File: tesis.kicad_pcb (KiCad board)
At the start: 2 copper layers, 12 parts, among them J1 Connector_RJ10, J2 Connector_RJ10, J3 Connector_RJ10, J4 Connector_RJ10, J5 Connector_RJ10, J6 Connector_RJ10, J7 Connector_RJ10, J8 Connector_RJ10, U1 ESP32-WROOM, U2 Interface_Expansion_PCF8574, U3 Interface_Expansion_TCA9548AP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

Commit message: Agrego v1.0 de SmartSaffron
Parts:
- removed J2, J3, J4, J5, J6, J7, J8: Connector_RJ10, 00_lib_fp:4P4C_narrow
- removed MOD1: RPi_GPIO, 00_lib_fp:RPi_fp
- removed U3: Interface_Expansion_TCA9548APWR, Package_SO:TSSOP-24_4.4x7.8mm_P0.65mm
- added AE501: Antenna_Shield, 00_lib_fp:U.FL_Molex_MCRF_73412-0110_Vertical, B.Cu at (62.4, 58.0)
- added BT501: CR2032, 00_lib_fp:BatteryHolder_ComfortableElectronic_CH273-2450_1x2450, F.Cu at (153.5, 80.8)
- added BT502: Battery_Cell, 00_lib_fp:BatteryHolder_Seiko_MS621F, B.Cu at (96.2, 66.2)
- added BZ601: Buzzer, 00_lib_fp:Buzzer_23x10, F.Cu at (167.1, 56.1)
- added C1: 10u, 00_lib_fp:C_0805_2012Metric_Pad1.18x1.45mm_HandSolder, B.Cu at (95.2, 127.3)
- added C101: 470uF/50V, 00_lib_fp:CP_Elec_10x10, F.Cu at (80.0, 126.7)
- added C102: 33u, 00_lib_fp:C_0805_2012Metric_Pad1.18x1.45mm_HandSolder, B.Cu at (97.6, 99.5)
- added C103: 470uF/50V, 00_lib_fp:CP_Elec_8x10.5, F.Cu at (87.9, 75.4)
- added C104: 470u/50V, 00_lib_fp:CP_Elec_8x10.5, F.Cu at (85.4, 115.9)
- added C105: 1u, 00_lib_fp:C_0805_2012Metric_Pad1.18x1.45mm_HandSolder, F.Cu at (85.4, 110.2)
- added C106: 33u, 00_lib_fp:C_0805_2012Metric_Pad1.18x1.45mm_HandSolder, B.Cu at (78.6, 99.4)
- added C107: 470uF/50V, 00_lib_fp:CP_Elec_8x10.5, F.Cu at (67.6, 75.4)
- added C108: 470uF/50V, 00_lib_fp:CP_Elec_8x10.5, F.Cu at (70.9, 115.9)
- added C109: 1u, 00_lib_fp:C_0805_2012Metric_Pad1.18x1.45mm_HandSolder, F.Cu at (69.9, 110.2)
- added C2: 100n, 00_lib_fp:C_0805_2012Metric_Pad1.18x1.45mm_HandSolder, B.Cu at (97.3, 127.3)
- added C201: 10u, 00_lib_fp:C_0805_2012Metric_Pad1.18x1.45mm_HandSolder, B.Cu at (170.9, 93.4)
- added C202: 100n, 00_lib_fp:C_0805_2012Metric_Pad1.18x1.45mm_HandSolder, B.Cu at (170.9, 91.0)
- added C3: 100n, 00_lib_fp:C_0805_2012Metric_Pad1.18x1.45mm_HandSolder, B.Cu at (92.1, 124.5)
- added C301: 100n, 00_lib_fp:C_0805_2012Metric_Pad1.18x1.45mm_HandSolder, F.Cu at (120.1, 50.1)
- added C302: 100n, 00_lib_fp:C_0805_2012Metric_Pad1.18x1.45mm_HandSolder, B.Cu at (144.5, 83.2)
- added C303: 100n, 00_lib_fp:C_0805_2012Metric_Pad1.18x1.45mm_HandSolder, B.Cu at (141.1, 92.4)
- added C304: 10u, 00_lib_fp:C_0805_2012Metric_Pad1.18x1.45mm_HandSolder, F.Cu at (118.6, 44.8)
- added C305: 100n, 00_lib_fp:C_0805_2012Metric_Pad1.18x1.45mm_HandSolder, F.Cu at (121.6, 44.8)
- added C401: 100n, 00_lib_fp:C_0805_2012Metric_Pad1.18x1.45mm_HandSolder, B.Cu at (116.7, 139.7)
- added C402: 100n, 00_lib_fp:C_0805_2012Metric_Pad1.18x1.45mm_HandSolder, B.Cu at (121.8, 139.7)
- added C403: 100n, 00_lib_fp:C_0805_2012Metric_Pad1.18x1.45mm_HandSolder, B.Cu at (126.3, 139.7)
- added C404: 100n, 00_lib_fp:C_0805_2012Metric_Pad1.18x1.45mm_HandSolder, B.Cu at (131.4, 139.7)
- added C405: 10u, 00_lib_fp:C_0805_2012Metric_Pad1.18x1.45mm_HandSolder, F.Cu at (108.6, 95.3)
- added C406: 100n, 00_lib_fp:C_0805_2012Metric_Pad1.18x1.45mm_HandSolder, F.Cu at (105.6, 95.3)
- added C407: 100n, 00_lib_fp:C_0805_2012Metric_Pad1.18x1.45mm_HandSolder, B.Cu at (136.9, 139.7)
- added C408: 100n, 00_lib_fp:C_0805_2012Metric_Pad1.18x1.45mm_HandSolder, B.Cu at (142.1, 139.7)
- added C409: 100n, 00_lib_fp:C_0805_2012Metric_Pad1.18x1.45mm_HandSolder, B.Cu at (147.2, 139.7)
- added C410: 100n, 00_lib_fp:C_0805_2012Metric_Pad1.18x1.45mm_HandSolder, B.Cu at (152.1, 139.7)
- added C501: 10u, 00_lib_fp:C_0805_2012Metric_Pad1.18x1.45mm_HandSolder, B.Cu at (179.0, 67.2)
- added C502: 100n, 00_lib_fp:C_0805_2012Metric_Pad1.18x1.45mm_HandSolder, B.Cu at (176.9, 67.2)
- added C503: 10u, 00_lib_fp:C_0805_2012Metric_Pad1.18x1.45mm_HandSolder, B.Cu at (175.2, 71.6)
- added C504: 100n, 00_lib_fp:C_0805_2012Metric_Pad1.18x1.45mm_HandSolder, B.Cu at (175.2, 73.8)
- added C505: 10u, 00_lib_fp:C_0805_2012Metric_Pad1.18x1.45mm_HandSolder, B.Cu at (77.9, 75.7)
- added C506: 100n, 00_lib_fp:C_0805_2012Metric_Pad1.18x1.45mm_HandSolder, B.Cu at (77.9, 73.4)
- added D101: DF06S, 00_lib_fp:Diode_Bridge_Vishay_DFSFlat, B.Cu at (79.3, 134.6)
- added D102: 1N5824, 00_lib_fp:D_SMB_Handsoldering, F.Cu at (95.1, 115.7)
- added D103: green, 00_lib_fp:LED_0805_2012Metric_Castellated, F.Cu at (87.4, 69.0)
- added D104: 1N5824, 00_lib_fp:D_SMB_Handsoldering, F.Cu at (61.9, 115.5)
- added D105: green, 00_lib_fp:LED_0805_2012Metric_Castellated, F.Cu at (75.9, 69.0)
- added D301: WS2812, 00_lib_fp:LED_WS2812_PLCC6_5.0x5.0mm_P1.6mm, B.Cu at (134.4, 83.9)
- added D302: WS2812, 00_lib_fp:LED_WS2812_PLCC6_5.0x5.0mm_P1.6mm, B.Cu at (134.4, 92.9)
- added D501: 1N5817, 00_lib_fp:D_MiniMELF_Handsoldering, B.Cu at (94.3, 71.5)
- added D502: LED, 00_lib_fp:LED_0805_2012Metric_Castellated, B.Cu at (70.5, 69.8)
- added G1: LOGO_SSaffron, 00_lib_fp:smart_saffron, F.Cu at (85.3, 53.2)
- added G2: LOGO_utn, 00_lib_fp:logo_utn, F.Cu at (117.2, 70.5)
- added G3: LOGO_azafran, 00_lib_fp:azafran, F.Cu at (134.1, 86.6)
- added G4: LOGO_arg, 00_lib_fp:argentina, F.Cu at (92.1, 134.2)
- added J201: RJ10, 00_lib_fp:4P4C_narrow, F.Cu at (197.1, 100.6)
- added J202: RJ10, 00_lib_fp:4P4C_narrow, F.Cu at (197.1, 87.9)
- added J203: RJ10, 00_lib_fp:4P4C_narrow, F.Cu at (197.1, 75.7)
- added J204: RJ10, 00_lib_fp:4P4C_narrow, F.Cu at (197.1, 63.5)
- added J205: RJ10, 00_lib_fp:4P4C_narrow, F.Cu at (197.1, 51.2)
- added J206: RJ10, 00_lib_fp:4P4C_narrow, F.Cu at (197.1, 113.0)
- added J207: RJ10, 00_lib_fp:4P4C_narrow, F.Cu at (197.1, 125.5)
- added J208: RJ10, 00_lib_fp:4P4C_narrow, F.Cu at (197.1, 137.7)
- added J301: BOOT_Mode, 00_lib_fp:PinHeader_1x02_P2.54mm_Vertical, F.Cu at (151.4, 63.5)
- added J302: Debug_PROG, 00_lib_fp:PinHeader_1x03_P2.54mm_Vertical, F.Cu at (150.9, 48.3)
- added J401: OUTPUT_SW, 00_lib_fp:TerminalBlock_Phoenix_MKDS-1,5-8-5.08_1x08_P5.08mm_Horizontal, F.Cu at (116.9, 133.7)
- added J402: COMMON, 00_lib_fp:TerminalBlock_Phoenix_MKDS-1,5-2-5.08_1x02_P5.08mm_Horizontal, F.Cu at (101.8, 133.7)
- added J602: Lights, 00_lib_fp:TerminalBlock_Phoenix_MKDS-1,5-4-5.08_1x04_P5.08mm_Horizontal, F.Cu at (162.9, 133.7)
- added JP1: jumper, 00_lib_fp:SolderJumper-2_P1.3mm_Open_RoundedPad1.0x1.5mm, B.Cu at (91.7, 137.0)
- added JP101: jumper, 00_lib_fp:SolderJumper-2_P1.3mm_Open_RoundedPad1.0x1.5mm, B.Cu at (99.2, 83.7)
- added JP102: jumper, 00_lib_fp:SolderJumper-2_P1.3mm_Open_RoundedPad1.0x1.5mm, B.Cu at (99.2, 77.9)
- added JP103: jumper, 00_lib_fp:SolderJumper-2_P1.3mm_Open_RoundedPad1.0x1.5mm, B.Cu at (99.2, 86.4)
- added JP104: jumper, 00_lib_fp:SolderJumper-2_P1.3mm_Open_RoundedPad1.0x1.5mm, B.Cu at (99.2, 92.0)
- added JP2: jumper, 00_lib_fp:SolderJumper-2_P1.3mm_Open_RoundedPad1.0x1.5mm, B.Cu at (91.8, 140.3)
- added L101: 33uH/5A, 00_lib_fp:Coil_ferrite, F.Cu at (86.9, 87.9)
- added L102: 33uH/5A, 00_lib_fp:Coil_ferrite, F.Cu at (67.1, 87.9)
- added L501: 27u, 00_lib_fp:L_0805_2012Metric_Pad1.15x1.40mm_HandSolder, B.Cu at (68.8, 59.1)
- added MH1: MountingHole, 00_lib_fp:MountingHole_3.2mm_M3_Pad_Via, F.Cu at (63.6, 138.7)
- added MH2: MountingHole, 00_lib_fp:MountingHole_3.2mm_M3_Pad_Via, F.Cu at (190.6, 138.7)
- added MH3: MountingHole, 00_lib_fp:MountingHole_3.2mm_M3_Pad_Via, F.Cu at (64.1, 65.7)
- added MH4: MountingHole, 00_lib_fp:MountingHole_3.2mm_M3_Pad_Via, F.Cu at (190.6, 46.7)
- added MOD301: RPi_GPIO, 00_lib_fp:PinSocket_2x20_P2.54mm_Vertical_SMD, B.Cu at (86.9, 48.8)
- added Q401: bss138, 00_lib_fp:SOT-23, B.Cu at (102.9, 116.9)
- added Q402: bss138, 00_lib_fp:SOT-23, B.Cu at (111.5, 116.9)
- added Q403: mac97a8, 00_lib_fp:TO-92_Inline, F.Cu at (101.6, 127.7)
- added Q404: mac97a8, 00_lib_fp:TO-92_Inline, F.Cu at (110.4, 127.7)
- added Q405: bss138, 00_lib_fp:SOT-23, B.Cu at (120.3, 116.9)
- added Q406: bss138, 00_lib_fp:SOT-23, B.Cu at (128.7, 116.9)
- added Q407: mac97a8, 00_lib_fp:TO-92_Inline, F.Cu at (119.0, 127.7)
- added Q408: mac97a8, 00_lib_fp:TO-92_Inline, F.Cu at (127.4, 127.7)
- added Q409: bss138, 00_lib_fp:SOT-23, B.Cu at (137.2, 116.9)
- added Q410: bss138, 00_lib_fp:SOT-23, B.Cu at (145.8, 116.9)
- added Q411: mac97a8, 00_lib_fp:TO-92_Inline, F.Cu at (135.9, 127.7)
- added Q412: mac97a8, 00_lib_fp:TO-92_Inline, F.Cu at (144.5, 127.7)
- added Q413: bss138, 00_lib_fp:SOT-23, B.Cu at (154.4, 116.9)
- added Q414: bss138, 00_lib_fp:SOT-23, B.Cu at (162.8, 116.9)
- added Q415: mac97a8, 00_lib_fp:TO-92_Inline, F.Cu at (153.1, 127.7)
- added Q416: mac97a8, 00_lib_fp:TO-92_Inline, F.Cu at (161.7, 127.7)
- added Q601: bss138, 00_lib_fp:SOT-23, F.Cu at (161.2, 94.5)
- added Q602: mac97a8, 00_lib_fp:TO-92_Inline, F.Cu at (174.5, 127.7)
- added Q603: bss138, 00_lib_fp:SOT-23, F.Cu at (166.2, 94.5)
- added Q604: bss138, 00_lib_fp:SOT-23, B.Cu at (168.7, 55.7)
- added Q605: mac97a8, 00_lib_fp:TO-92_Inline, F.Cu at (168.4, 127.7)
- added Q606: bss138, 00_lib_fp:SOT-23, F.Cu at (171.2, 94.5)
- added Q607: mac97a8, 00_lib_fp:TO-92_Inline, F.Cu at (180.6, 127.7)
- added R1: R, 00_lib_fp:R_0805_2012Metric_Pad1.20x1.40mm_HandSolder, B.Cu at (94.0, 122.4)
- added R101: 1k5, 00_lib_fp:R_0805_2012Metric_Pad1.20x1.40mm_HandSolder, B.Cu at (81.6, 93.7)
- added R102: 0, 00_lib_fp:R_0805_2012Metric_Pad1.20x1.40mm_HandSolder, B.Cu at (85.7, 93.7)
- added R103: 0, 00_lib_fp:R_0805_2012Metric_Pad1.20x1.40mm_HandSolder, B.Cu at (81.6, 91.5)
- added R104: 8k2, 00_lib_fp:R_0805_2012Metric_Pad1.20x1.40mm_HandSolder, B.Cu at (89.7, 93.7)
- added R105: 2k2, 00_lib_fp:R_0805_2012Metric_Pad1.20x1.40mm_HandSolder, F.Cu at (83.6, 68.9)
- added R106: 4k7, 00_lib_fp:R_0805_2012Metric_Pad1.20x1.40mm_HandSolder, B.Cu at (62.1, 93.7)
- added R107: 0, 00_lib_fp:R_0805_2012Metric_Pad1.20x1.40mm_HandSolder, B.Cu at (66.1, 93.7)
- added R108: 0, 00_lib_fp:R_0805_2012Metric_Pad1.20x1.40mm_HandSolder, B.Cu at (62.1, 91.5)
- added R109: 15k, 00_lib_fp:R_0805_2012Metric_Pad1.20x1.40mm_HandSolder, B.Cu at (70.1, 93.7)
- added R110: 2k2, 00_lib_fp:R_0805_2012Metric_Pad1.20x1.40mm_HandSolder, F.Cu at (72.4, 68.9)
- added R2: R, 00_lib_fp:R_0805_2012Metric_Pad1.20x1.40mm_HandSolder, B.Cu at (94.0, 120.4)
- added R201: 10k, 00_lib_fp:R_0805_2012Metric_Pad1.20x1.40mm_HandSolder, B.Cu at (190.5, 100.1)
- added R202: 10k, 00_lib_fp:R_0805_2012Metric_Pad1.20x1.40mm_HandSolder, B.Cu at (190.5, 98.0)
- added R203: 10k, 00_lib_fp:R_0805_2012Metric_Pad1.20x1.40mm_HandSolder, B.Cu at (190.6, 87.6)
- added R204: 10k, 00_lib_fp:R_0805_2012Metric_Pad1.20x1.40mm_HandSolder, B.Cu at (190.6, 85.6)
- added R205: 10k, 00_lib_fp:R_0805_2012Metric_Pad1.20x1.40mm_HandSolder, B.Cu at (190.6, 75.2)
- added R206: 10k, 00_lib_fp:R_0805_2012Metric_Pad1.20x1.40mm_HandSolder, B.Cu at (190.6, 73.2)
- added R207: 4k7, 00_lib_fp:R_0805_2012Metric_Pad1.20x1.40mm_HandSolder, B.Cu at (186.0, 90.5)
- added R208: 4k7, 00_lib_fp:R_0805_2012Metric_Pad1.20x1.40mm_HandSolder, B.Cu at (183.9, 90.5)
- added R209: 10k, 00_lib_fp:R_0805_2012Metric_Pad1.20x1.40mm_HandSolder, B.Cu at (190.6, 63.0)
- added R210: 10k, 00_lib_fp:R_0805_2012Metric_Pad1.20x1.40mm_HandSolder, B.Cu at (190.6, 60.9)
- added R211: 10k, 00_lib_fp:R_0805_2012Metric_Pad1.20x1.40mm_HandSolder, F.Cu at (175.3, 97.4)
- added R212: 10k, 00_lib_fp:R_0805_2012Metric_Pad1.20x1.40mm_HandSolder, F.Cu at (177.2, 92.2)
- added R213: 10k, 00_lib_fp:R_0805_2012Metric_Pad1.20x1.40mm_HandSolder, F.Cu at (177.2, 95.1)
- added R214: 10k, 00_lib_fp:R_0805_2012Metric_Pad1.20x1.40mm_HandSolder, F.Cu at (177.2, 89.1)
- added R215: 10k, 00_lib_fp:R_0805_2012Metric_Pad1.20x1.40mm_HandSolder, B.Cu at (190.6, 54.2)
- added R216: 10k, 00_lib_fp:R_0805_2012Metric_Pad1.20x1.40mm_HandSolder, B.Cu at (190.6, 52.2)
- added R217: 10k, 00_lib_fp:R_0805_2012Metric_Pad1.20x1.40mm_HandSolder, F.Cu at (179.2, 92.2)
- added R218: 10k, 00_lib_fp:R_0805_2012Metric_Pad1.20x1.40mm_HandSolder, F.Cu at (179.2, 95.1)
- added R219: 10k, 00_lib_fp:R_0805_2012Metric_Pad1.20x1.40mm_HandSolder, F.Cu at (179.2, 89.1)
- added R220: 10k, 00_lib_fp:R_0805_2012Metric_Pad1.20x1.40mm_HandSolder, B.Cu at (190.5, 112.4)
- added R221: 10k, 00_lib_fp:R_0805_2012Metric_Pad1.20x1.40mm_HandSolder, B.Cu at (190.5, 110.4)
- added R222: 10k, 00_lib_fp:R_0805_2012Metric_Pad1.20x1.40mm_HandSolder, B.Cu at (190.6, 125.0)
- added R223: 10k, 00_lib_fp:R_0805_2012Metric_Pad1.20x1.40mm_HandSolder, B.Cu at (190.6, 123.0)
- added R224: 10k, 00_lib_fp:R_0805_2012Metric_Pad1.20x1.40mm_HandSolder, B.Cu at (190.6, 133.2)
- added R225: 10k, 00_lib_fp:R_0805_2012Metric_Pad1.20x1.40mm_HandSolder, B.Cu at (190.6, 131.2)
- added R301: 10k, 00_lib_fp:R_0805_2012Metric_Pad1.20x1.40mm_HandSolder, F.Cu at (120.2, 47.9)
- added R401: 1k, 00_lib_fp:R_0805_2012Metric_Pad1.20x1.40mm_HandSolder, B.Cu at (100.0, 123.9)
- added R402: 1k, 00_lib_fp:R_0805_2012Metric_Pad1.20x1.40mm_HandSolder, B.Cu at (108.8, 123.9)
- added R403: 470, 00_lib_fp:R_0805_2012Metric_Pad1.20x1.40mm_HandSolder, B.Cu at (116.6, 137.5)
- added R404: 470, 00_lib_fp:R_0805_2012Metric_Pad1.20x1.40mm_HandSolder, B.Cu at (121.8, 137.5)
- added R405: 1k, 00_lib_fp:R_0805_2012Metric_Pad1.20x1.40mm_HandSolder, B.Cu at (105.0, 110.1)
- added R406: 470, 00_lib_fp:R_0805_2012Metric_Pad1.20x1.40mm_HandSolder, B.Cu at (100.7, 110.1)
- added R407: 1k, 00_lib_fp:R_0805_2012Metric_Pad1.20x1.40mm_HandSolder, B.Cu at (113.8, 110.1)
- added R408: 470, 00_lib_fp:R_0805_2012Metric_Pad1.20x1.40mm_HandSolder, B.Cu at (109.4, 110.1)
- added R409: 4k7, 00_lib_fp:R_0805_2012Metric_Pad1.20x1.40mm_HandSolder, F.Cu at (112.9, 85.6)
- added R410: 4k7, 00_lib_fp:R_0805_2012Metric_Pad1.20x1.40mm_HandSolder, F.Cu at (115.0, 85.6)
- added R411: 10k, 00_lib_fp:R_0805_2012Metric_Pad1.20x1.40mm_HandSolder, F.Cu at (108.4, 103.4)
- added R412: 10k, 00_lib_fp:R_0805_2012Metric_Pad1.20x1.40mm_HandSolder, F.Cu at (105.6, 103.4)
- added R413: 10k, 00_lib_fp:R_0805_2012Metric_Pad1.20x1.40mm_HandSolder, F.Cu at (102.8, 103.4)
- added R414: 10k, 00_lib_fp:R_0805_2012Metric_Pad1.20x1.40mm_HandSolder, F.Cu at (108.4, 105.4)
- added R415: 10k, 00_lib_fp:R_0805_2012Metric_Pad1.20x1.40mm_HandSolder, F.Cu at (105.6, 105.4)
- added R416: 10k, 00_lib_fp:R_0805_2012Metric_Pad1.20x1.40mm_HandSolder, F.Cu at (102.8, 105.4)
- added R417: 1k, 00_lib_fp:R_0805_2012Metric_Pad1.20x1.40mm_HandSolder, B.Cu at (117.4, 123.9)
- added R418: 1k, 00_lib_fp:R_0805_2012Metric_Pad1.20x1.40mm_HandSolder, B.Cu at (125.8, 123.9)
- added R419: 470, 00_lib_fp:R_0805_2012Metric_Pad1.20x1.40mm_HandSolder, B.Cu at (126.2, 137.5)
- added R420: 470, 00_lib_fp:R_0805_2012Metric_Pad1.20x1.40mm_HandSolder, B.Cu at (131.4, 137.6)
- added R421: 1k, 00_lib_fp:R_0805_2012Metric_Pad1.20x1.40mm_HandSolder, B.Cu at (122.4, 110.1)
- added R422: 470, 00_lib_fp:R_0805_2012Metric_Pad1.20x1.40mm_HandSolder, B.Cu at (118.2, 110.1)
- added R423: 1k, 00_lib_fp:R_0805_2012Metric_Pad1.20x1.40mm_HandSolder, B.Cu at (130.8, 110.1)
- added R424: 470, 00_lib_fp:R_0805_2012Metric_Pad1.20x1.40mm_HandSolder, B.Cu at (126.6, 110.1)
- added R425: 1k, 00_lib_fp:R_0805_2012Metric_Pad1.20x1.40mm_HandSolder, B.Cu at (134.3, 123.9)
- added R426: 1k, 00_lib_fp:R_0805_2012Metric_Pad1.20x1.40mm_HandSolder, B.Cu at (142.9, 123.9)
- added R427: 470, 00_lib_fp:R_0805_2012Metric_Pad1.20x1.40mm_HandSolder, B.Cu at (136.9, 137.6)
- added R428: 470, 00_lib_fp:R_0805_2012Metric_Pad1.20x1.40mm_HandSolder, B.Cu at (142.1, 137.5)
- added R429: 1k, 00_lib_fp:R_0805_2012Metric_Pad1.20x1.40mm_HandSolder, B.Cu at (139.4, 110.1)
- added R430: 470, 00_lib_fp:R_0805_2012Metric_Pad1.20x1.40mm_HandSolder, B.Cu at (135.0, 110.1)
- added R431: 1k, 00_lib_fp:R_0805_2012Metric_Pad1.20x1.40mm_HandSolder, B.Cu at (147.9, 110.1)
- added R432: 470, 00_lib_fp:R_0805_2012Metric_Pad1.20x1.40mm_HandSolder, B.Cu at (143.6, 110.1)
- added R433: 1k, 00_lib_fp:R_0805_2012Metric_Pad1.20x1.40mm_HandSolder, B.Cu at (151.6, 123.9)
- added R434: 1k, 00_lib_fp:R_0805_2012Metric_Pad1.20x1.40mm_HandSolder, B.Cu at (160.1, 123.9)
- added R435: 470, 00_lib_fp:R_0805_2012Metric_Pad1.20x1.40mm_HandSolder, B.Cu at (147.2, 137.6)
- added R436: 470, 00_lib_fp:R_0805_2012Metric_Pad1.20x1.40mm_HandSolder, B.Cu at (152.1, 137.6)
- added R437: 1k, 00_lib_fp:R_0805_2012Metric_Pad1.20x1.40mm_HandSolder, B.Cu at (156.3, 110.1)
- added R438: 470, 00_lib_fp:R_0805_2012Metric_Pad1.20x1.40mm_HandSolder, B.Cu at (152.2, 110.1)
- added R439: 1k, 00_lib_fp:R_0805_2012Metric_Pad1.20x1.40mm_HandSolder, B.Cu at (165.1, 110.1)
- added R440: 470, 00_lib_fp:R_0805_2012Metric_Pad1.20x1.40mm_HandSolder, B.Cu at (160.8, 110.1)
- added R501: 1k, 00_lib_fp:R_0805_2012Metric_Pad1.20x1.40mm_HandSolder, B.Cu at (156.3, 61.4)
- added R502: 1k, 00_lib_fp:R_0805_2012Metric_Pad1.20x1.40mm_HandSolder, B.Cu at (158.9, 61.4)
- added R503: 10.5, 00_lib_fp:R_0805_2012Metric_Pad1.20x1.40mm_HandSolder, B.Cu at (72.0, 60.3)
- added R504: 1k, 00_lib_fp:R_0805_2012Metric_Pad1.20x1.40mm_HandSolder, B.Cu at (72.7, 69.8)
- added R505: 10k, 00_lib_fp:R_0805_2012Metric_Pad1.20x1.40mm_HandSolder, B.Cu at (162.9, 83.8)
- added R506: 10k, 00_lib_fp:R_0805_2012Metric_Pad1.20x1.40mm_HandSolder, B.Cu at (165.9, 83.8)
- added R507: 10k, 00_lib_fp:R_0805_2012Metric_Pad1.20x1.40mm_HandSolder, B.Cu at (168.9, 83.8)
- added R508: 10k, 00_lib_fp:R_0805_2012Metric_Pad1.20x1.40mm_HandSolder, B.Cu at (162.9, 81.8)
- added R509: 10k, 00_lib_fp:R_0805_2012Metric_Pad1.20x1.40mm_HandSolder, B.Cu at (165.9, 81.8)
- added R510: 10k, 00_lib_fp:R_0805_2012Metric_Pad1.20x1.40mm_HandSolder, B.Cu at (168.9, 81.8)
- added R601: 1k, 00_lib_fp:R_0805_2012Metric_Pad1.20x1.40mm_HandSolder, F.Cu at (160.2, 100.6)
- added R602: 1k, 00_lib_fp:R_0805_2012Metric_Pad1.20x1.40mm_HandSolder, B.Cu at (173.0, 124.6)
- added R603: 1k, 00_lib_fp:R_0805_2012Metric_Pad1.20x1.40mm_HandSolder, F.Cu at (171.1, 116.9)
- added R604: 470, 00_lib_fp:R_0805_2012Metric_Pad1.20x1.40mm_HandSolder, F.Cu at (173.3, 116.9)
- added R605: 1k, 00_lib_fp:R_0805_2012Metric_Pad1.20x1.40mm_HandSolder, B.Cu at (163.5, 55.8)
- added R606: 1k, 00_lib_fp:R_0805_2012Metric_Pad1.20x1.40mm_HandSolder, F.Cu at (165.2, 100.5)
- added R607: 1k, 00_lib_fp:R_0805_2012Metric_Pad1.20x1.40mm_HandSolder, B.Cu at (166.9, 124.6)
- added R608: 1k, 00_lib_fp:R_0805_2012Metric_Pad1.20x1.40mm_HandSolder, B.Cu at (165.6, 55.8)
- added R609: 1k, 00_lib_fp:R_0805_2012Metric_Pad1.20x1.40mm_HandSolder, F.Cu at (164.6, 106.5)
- added R610: 470, 00_lib_fp:R_0805_2012Metric_Pad1.20x1.40mm_HandSolder, F.Cu at (166.7, 106.5)
- added R611: 1k, 00_lib_fp:R_0805_2012Metric_Pad1.20x1.40mm_HandSolder, F.Cu at (170.2, 100.5)
- added R612: 1k, 00_lib_fp:R_0805_2012Metric_Pad1.20x1.40mm_HandSolder, B.Cu at (179.1, 124.6)
- added R613: 1k, 00_lib_fp:R_0805_2012Metric_Pad1.20x1.40mm_HandSolder, F.Cu at (179.3, 106.7)
- added R614: 470, 00_lib_fp:R_0805_2012Metric_Pad1.20x1.40mm_HandSolder, F.Cu at (181.4, 106.7)
- added U101: XL4005E1, 00_lib_fp:TO-263-5_TabPin3, B.Cu at (88.1, 102.2)
- added U102: XL4005E1, 00_lib_fp:TO-263-5_TabPin3, B.Cu at (68.6, 102.2)
- added U201: TCA9548APWR, 00_lib_fp:TSSOP-24_4.4x7.8mm_P0.65mm, B.Cu at (177.8, 92.5)
- added U301: ESP32-WROOM, 00_lib_fp:ESP32-WROOM, F.Cu at (134.6, 49.7)
- added U401: MOC3043, 00_lib_fp:DIP-6_W7.62mm_LongPads, F.Cu at (105.4, 112.9)
- added U402: MOC3043, 00_lib_fp:DIP-6_W7.62mm_LongPads, F.Cu at (114.1, 112.9)
- added U403: PCF8574, 00_lib_fp:SOIC-16W_7.5x10.3mm_P1.27mm, F.Cu at (116.4, 95.6)
- added U404: MOC3043, 00_lib_fp:DIP-6_W7.62mm_LongPads, F.Cu at (122.8, 112.9)
- added U405: MOC3043, 00_lib_fp:DIP-6_W7.62mm_LongPads, F.Cu at (131.2, 112.9)
- added U406: MOC3043, 00_lib_fp:DIP-6_W7.62mm_LongPads, F.Cu at (139.7, 112.9)
- added U407: MOC3043, 00_lib_fp:DIP-6_W7.62mm_LongPads, F.Cu at (148.3, 112.9)
- added U408: MOC3043, 00_lib_fp:DIP-6_W7.62mm_LongPads, F.Cu at (156.9, 112.9)
- added U409: MOC3043, 00_lib_fp:DIP-6_W7.62mm_LongPads, F.Cu at (165.5, 112.9)
- added U501: DS3231M, 00_lib_fp:SOIC-16W_7.5x10.3mm_P1.27mm, B.Cu at (166.4, 66.9)
- added U502: NEO-6M, 00_lib_fp:ublox_NEO, B.Cu at (81.2, 63.9)
- added U503: AT24C32, 00_lib_fp:TSSOP-8_4.4x3mm_P0.65mm, B.Cu at (95.7, 59.9)
- added U504: AT24C32, 00_lib_fp:SOIC-8_3.9x4.9mm_P1.27mm, B.Cu at (166.3, 76.4)
- added U601: 4N35, 00_lib_fp:SMDIP-6_W7.62mm, F.Cu at (179.7, 117.9)
- added U602: 4N35, 00_lib_fp:SMDIP-6_W7.62mm, F.Cu at (173.0, 107.7)
- added U603: 4N35, 00_lib_fp:SMDIP-6_W7.62mm, F.Cu at (187.6, 107.7)
- J1: value Connector_RJ10 -> VAC_IN; footprint 00_lib_fp:4P4C_narrow -> 00_lib_fp:TerminalBlock_Phoenix_MKDS-1,5-2-5.08_1x02_P5.08mm_Horizontal
- U1: value ESP32-WROOM -> ACS712-05; footprint 00_lib_fp:ESP32-WROOM -> 00_lib_fp:SOIC-8_3.9x4.9mm_P1.27mm; moved to B.Cu
- U2: value Interface_Expansion_PCF8574 -> LM358; footprint 00_lib_fp:SOIC-16W_7.5x10.3mm_P1.27mm -> 00_lib_fp:SOIC-8_3.9x4.9mm_P1.27mm; moved to B.Cu
- moved J1 204.1 mm to (67.8, 127.0), turned to 270 degrees
- moved U1 146.6 mm to (91.2, 131.0), turned to 90 degrees
- moved U2 123.5 mm to (92.3, 115.4), turned to 180 degrees
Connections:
- J1 pad 1: (no net) -> /monitor/[AGND_in]
- J1 pad 2: (no net) -> /[24VAC_main]
- U1 pad 1: (no net) -> /[AGND_main]
- U1 pad 2: (no net) -> /[AGND_main]
- U1 pad 3: (no net) -> /monitor/[AGND_in]
- U1 pad 4: (no net) -> /monitor/[AGND_in]
- U1 pad 5: (no net) -> GND
- U1 pad 6: (no net) -> Net-(C3-Pad1)
- U1 pad 7: (no net) -> Net-(R1-Pad1)
- U1 pad 8: (no net) -> +5V
- U2 pad 1: (no net) -> /Core/[ADC_uC]
- U2 pad 2: (no net) -> /Core/[ADC_uC]
- U2 pad 3: (no net) -> Net-(R1-Pad2)
- U2 pad 4: (no net) -> GND
- U2 pad 8: (no net) -> +5V
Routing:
- net GND: track 0.00 -> 1267.1 mm, vias 0 -> 123
- net +3V3: track 0.00 -> 679.0 mm, vias 0 -> 39
- net +5V: track 0.00 -> 385.9 mm, vias 0 -> 42
- net /[24VAC_main]: track 0.00 -> 235.3 mm, vias 0 -> 9
- net /Core/[ADC_uC]: track 0.00 -> 120.1 mm, vias 0 -> 1
- net /Core/[SDA1_uC]: track 0.00 -> 81.2 mm, vias 0 -> 1
- net /Core/[SCL1_uC]: track 0.00 -> 72.6 mm, vias 0 -> 1
- net /Outputs/P4: track 0.00 -> 68.5 mm, vias 0 -> 1
- net /Alerts/[GREEN_ALERT_in]: track 0.00 -> 65.8 mm, vias 0 -> 2
- net /inputs/SD4: track 0.00 -> 65.2 mm, vias 0 -> 2
- net /Outputs/P5: track 0.00 -> 64.3 mm, vias 0 -> 1
- net /GPS&RTC/[RX_gps]: track 0.00 -> 61.9 mm, vias 0 -> 1
- net /inputs/SC4: track 0.00 -> 61.9 mm
- net /Alerts/[YELLOW_ALERT_in]: track 0.00 -> 61.7 mm, vias 0 -> 2
- net /inputs/SD5: track 0.00 -> 58.5 mm, vias 0 -> 2
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- added copper zone on B.Cu, net (none)
- added copper zone on F.Cu, net (none)
- added copper zone on B.Cu, net +3V3
- added copper zone on PWR, net +3V3
- added copper zone on B.Cu, net +5V
- added copper zone on PWR, net +5V
- added copper zone on B.Cu, net /[24VAC_main]
- added copper zone on PWR, net /[24VAC_main]
- added copper zone on B.Cu, net /[AGND_main]
- added copper zone on PWR, net /[AGND_main]
- added copper zone on B.Cu, net /monitor/[AGND_in]
- added copper zone on F.Cu, net /monitor/[AGND_in]
- added copper zone on B.Cu, net 24V_DC
- added copper zone on F.Cu, net 24V_DC
- added copper zone on PWR, net 24V_DC
- added copper zone on B.Cu, net GND
- added copper zone on F.Cu, net GND
- added copper zone on GND, net GND
- added copper zone on B.Cu, net Net-(C102-Pad1)
- added copper zone on F.Cu, net Net-(C102-Pad1)
- added copper zone on PWR, net Net-(C102-Pad1)
- added copper zone on B.Cu, net Net-(C106-Pad1)
- added copper zone on F.Cu, net Net-(C106-Pad1)
- added copper zone on PWR, net Net-(C106-Pad1)
- added copper zone on B.Cu, net Net-(D102-Pad1)
- added copper zone on F.Cu, net Net-(D102-Pad1)
- added copper zone on B.Cu, net Net-(D104-Pad1)
- added copper zone on F.Cu, net Net-(D104-Pad1)
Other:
- board outline added: 150 x 100 mm
- copper layers 2 -> 4
- net class Default: trace_width 0.25 -> 0.4; via_dia 0.8 -> 1; via_drill 0.4 -> 0.6
- board text added: "+3V3"
- board text added: "+5V"
- board text added: "4121"
- board text added: "BOOT MODE"
- board text added: "Castro"
- board text added: "Cussa"
- board text added: "GND"
- board text added: "Grupo 6/21"
- board text added: "Navarro"
- board text added: "Nobile"
- board text added: "RX"
- board text added: "TX"
- board text added: "v1.0"

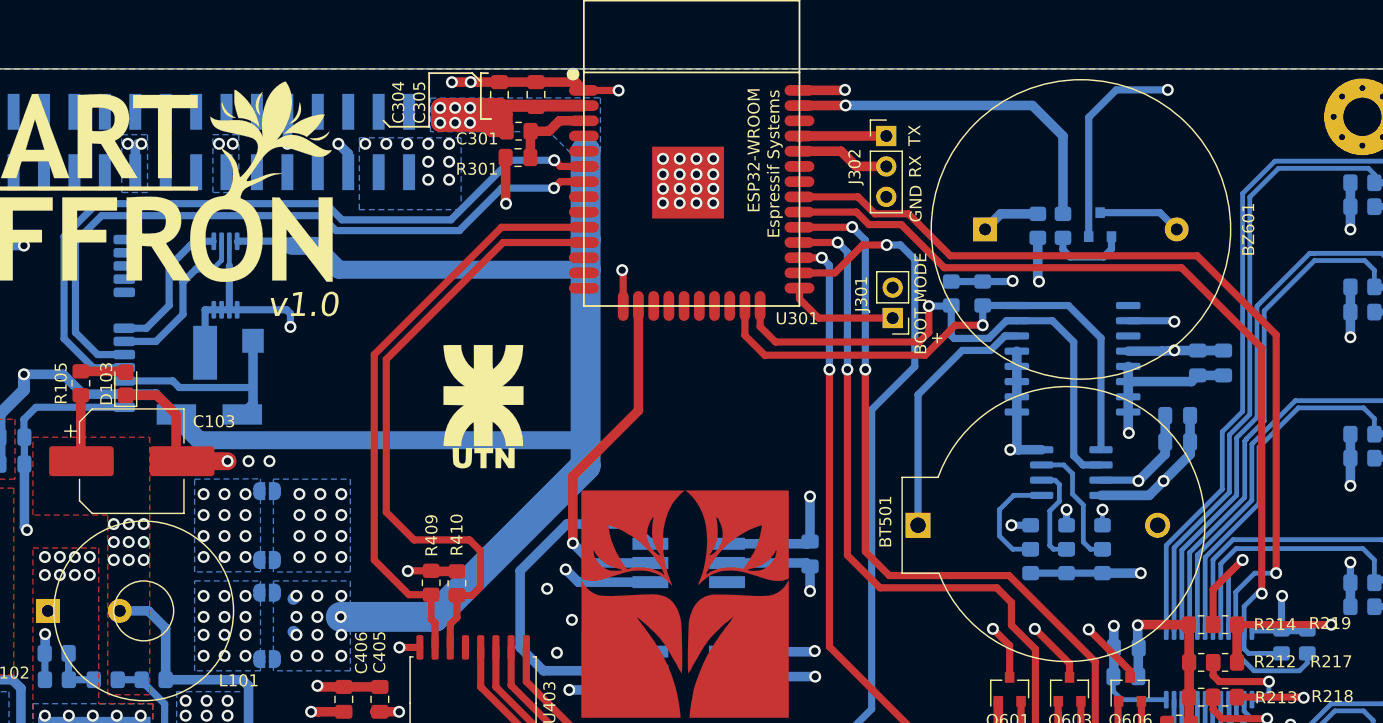
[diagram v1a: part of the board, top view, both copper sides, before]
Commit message: Fixes PCB, reset esp32
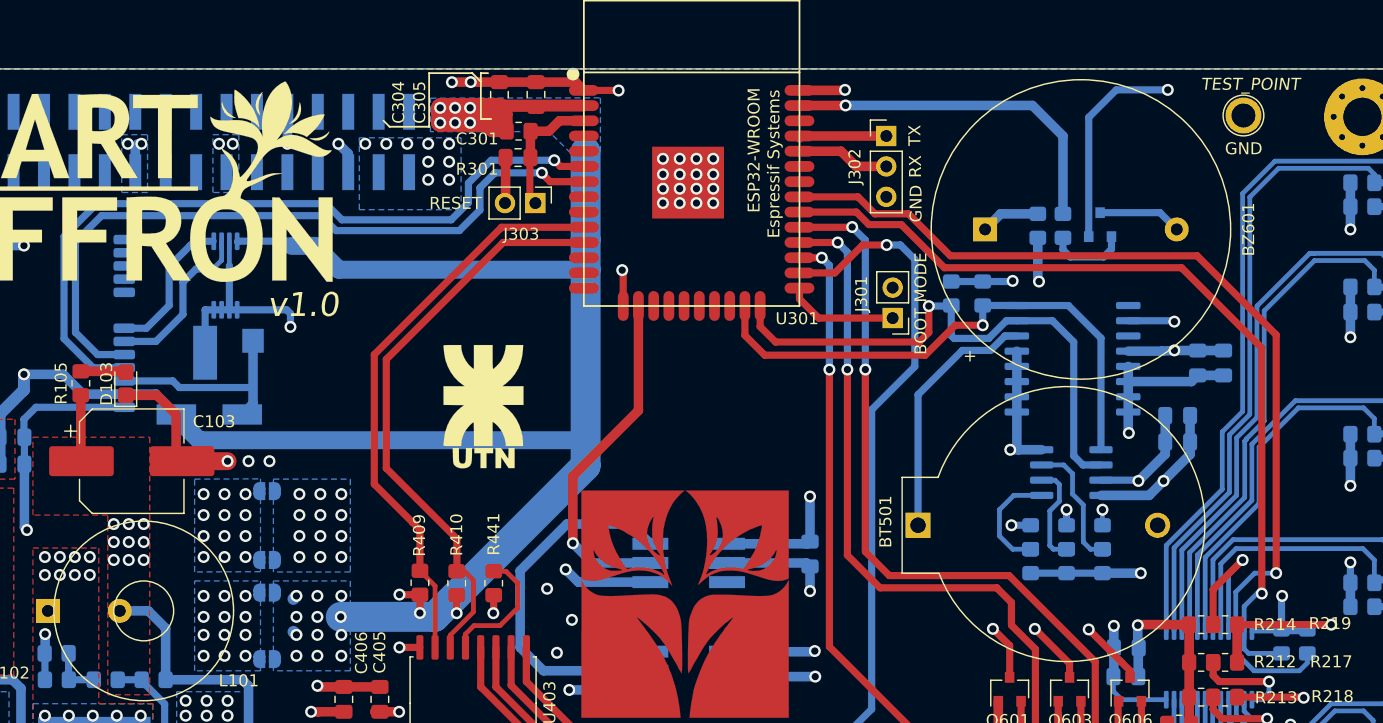
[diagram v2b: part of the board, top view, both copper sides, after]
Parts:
- added J303: RESET, 00_lib_fp:PinHeader_1x02_P2.54mm_Vertical, F.Cu at (121.6, 53.9)
- added R441: 10k, 00_lib_fp:R_0805_2012Metric_Pad1.20x1.40mm_HandSolder, F.Cu at (118.1, 85.6)
- added REF**: KiCad-Logo2_6mm_SilkScreen, Symbol:KiCad-Logo2_6mm_SilkScreen, B.Cu at (177.8, 137.4)
- added TP1: TestPoint, 00_lib_fp:TestPoint_Plated_Hole_D2.0mm, F.Cu at (180.7, 46.6)
- moved R409 0.94 mm to (111.9, 85.6), turned to 90 degrees
- turned R410 to 90 degrees
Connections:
- U403 pad 13: (no net) -> Net-(R441-Pad2)
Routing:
- net Net-(R441-Pad2): track 0.00 -> 10.9 mm
- net Net-(C301-Pad1): track 6.96 -> 11.0 mm
- net /Core/[SCL2_uC]: track 52.3 -> 48.8 mm
- net +3V3: track 679.0 -> 680.9 mm, vias 39 -> 42
- net /Core/[RX_uC]: track 58.0 -> 59.7 mm
- net /Core/[SDA2_uC]: track 49.5 -> 48.5 mm
- net GND: track 1267.1 -> 1266.0 mm, vias 123 -> 122
- net /GPS&RTC/[RX_gps]: track 61.9 -> 62.9 mm
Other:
- board text added: "RESET"
- board text added: "TEST_POINT"

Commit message: Revision
    * Acomodo los datos de F.Fab y B.Fab
    * Genero ibom
    * Exporto PDF e imagenes
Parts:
- C101, C108: value 470uF/50V -> 470u/50V
- R1: value R -> 1k7
- R2: value R -> 3k3

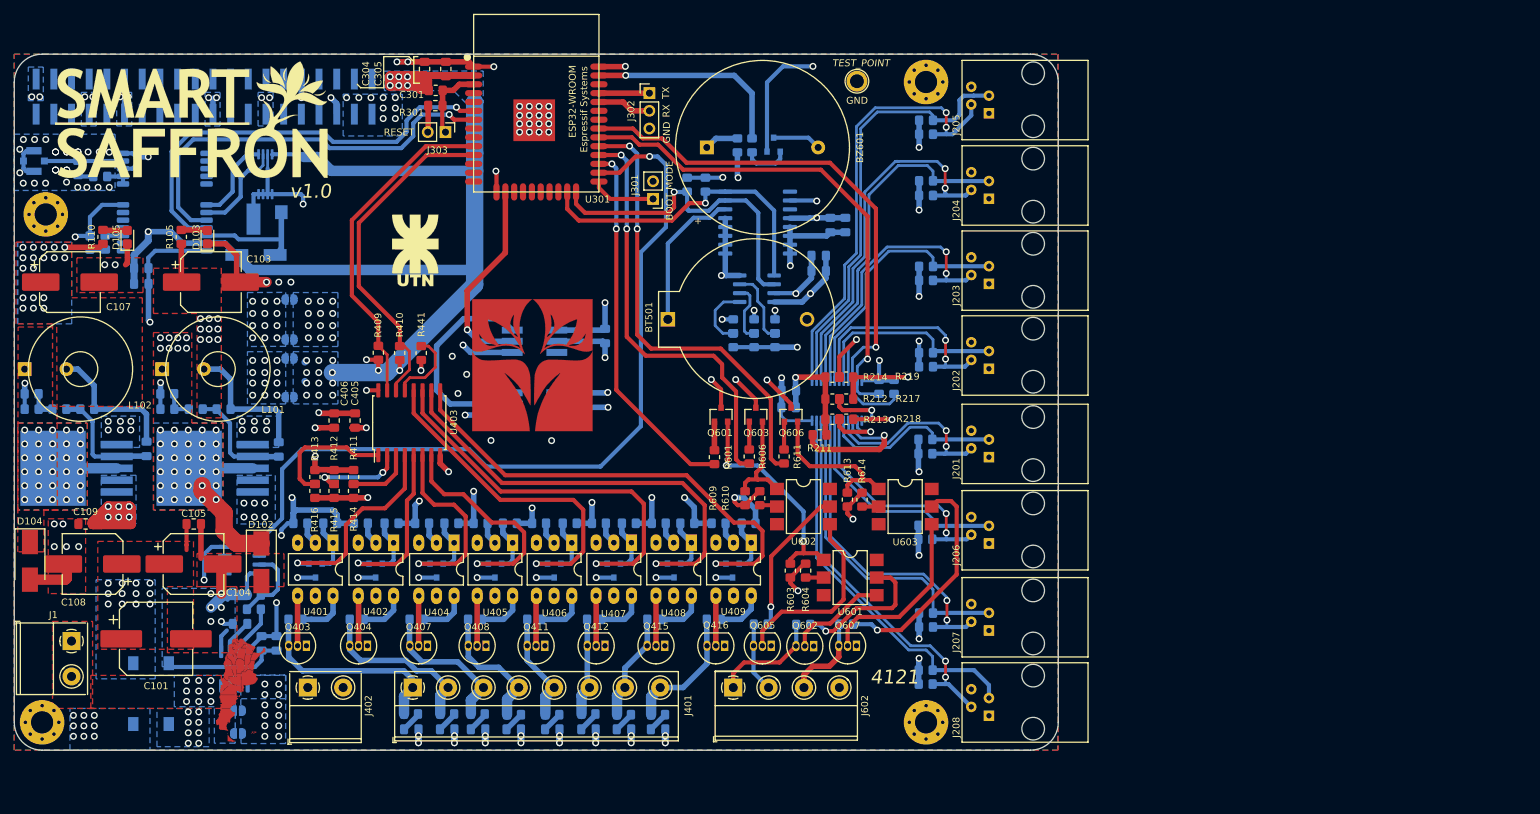
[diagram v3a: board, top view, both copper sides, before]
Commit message: Fix por revision grupal
    *Fix de memoria de i2c, mal sda y scl
    *Fix inpunts sda y scl
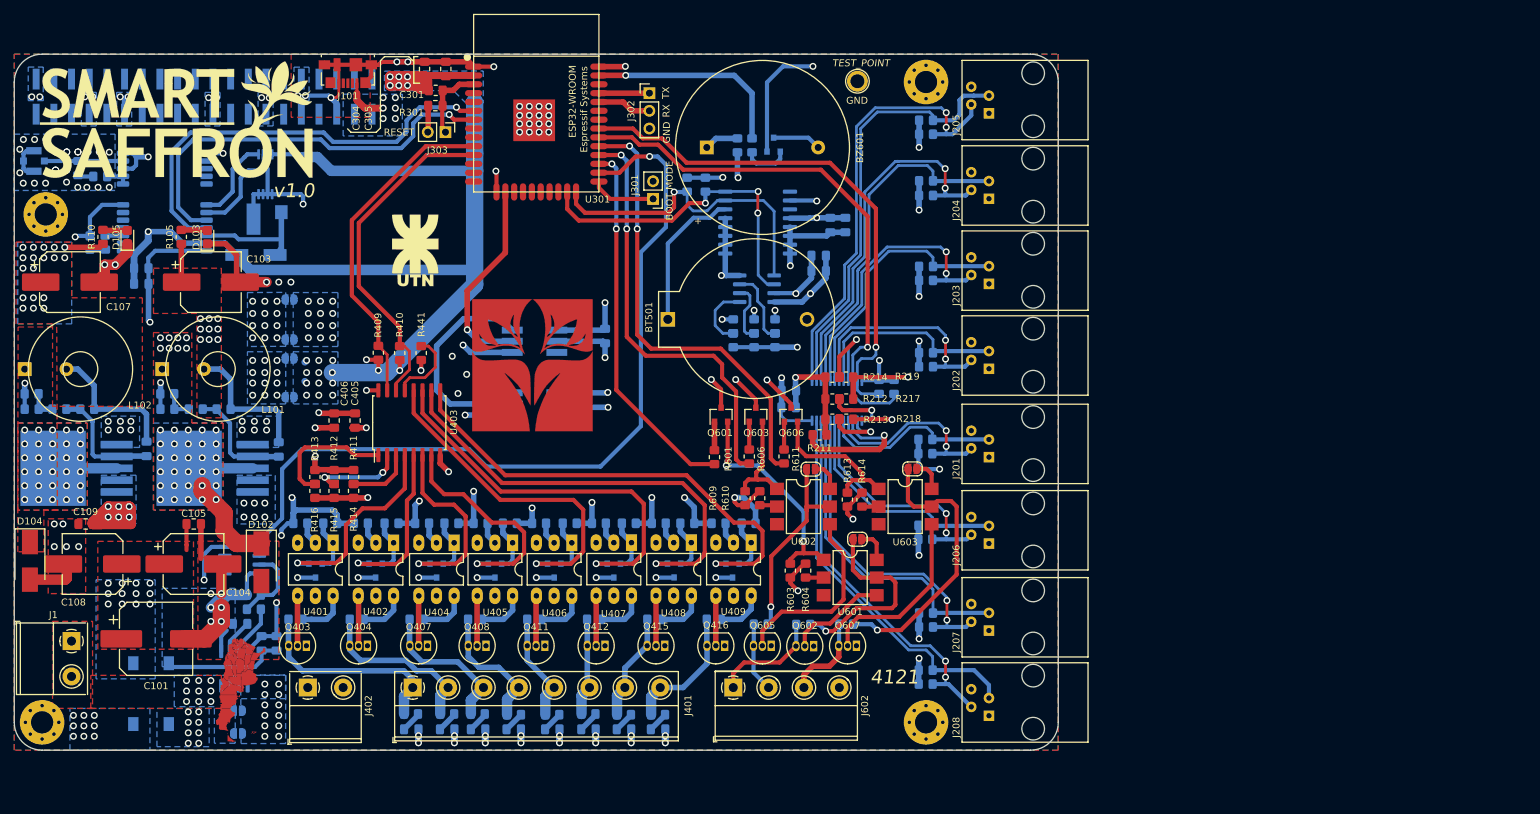
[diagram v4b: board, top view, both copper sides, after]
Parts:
- added J101: USB_B_Micro, 00_lib_fp:USB_Micro-B_Molex_47346-0001, F.Cu at (107.5, 45.4)
- added JP601: jumper, 00_lib_fp:SolderJumper-2_P1.3mm_Open_RoundedPad1.0x1.5mm, F.Cu at (180.8, 112.4)
- added JP602: jumper, 00_lib_fp:SolderJumper-2_P1.3mm_Open_RoundedPad1.0x1.5mm, F.Cu at (174.1, 102.3)
- added JP603: jumper, 00_lib_fp:SolderJumper-2_P1.3mm_Open_RoundedPad1.0x1.5mm, F.Cu at (188.7, 102.3)
- moved G1 2.17 mm to (83.1, 53.2)
- moved TP1 0.07 mm to (180.8, 46.6)
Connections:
- R207 pad 2: /Core/[SDA1_uC] -> /Core/[SCL1_uC]
- R208 pad 2: /Core/[SCL1_uC] -> /Core/[SDA1_uC]
- U201 pad 22: /Core/[SDA1_uC] -> /Core/[SCL1_uC]
- U201 pad 23: /Core/[SCL1_uC] -> /Core/[SDA1_uC]
- U504 pad 5: /Core/[SCL3_uC] -> /Core/[SDA3_uC]
- U504 pad 6: /Core/[SDA3_uC] -> /Core/[SCL3_uC]
- U601 pad 6: (no net) -> Net-(JP601-Pad1)
- U602 pad 6: (no net) -> Net-(JP602-Pad1)
- U603 pad 6: (no net) -> Net-(JP603-Pad1)
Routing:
- net GND: track 1266.0 -> 1300.4 mm, vias 122 -> 123
- net +3V3: track 680.9 -> 693.9 mm
- net Net-(JP603-Pad2): track 32.6 -> 40.9 mm
- net Net-(JP601-Pad2): track 20.4 -> 28.7 mm
- net Net-(JP602-Pad2): track 21.4 -> 28.5 mm
- net /Core/[SDA1_uC]: track 81.2 -> 76.0 mm
- net /Core/[SCL1_uC]: track 72.6 -> 77.8 mm
- net +5V: track 385.9 -> 390.9 mm, vias 42 -> 37
- net Net-(JP601-Pad1): track 0.00 -> 4.74 mm
- net /inputs/SD5: track 58.5 -> 53.8 mm
- net Net-(JP603-Pad1): track 0.00 -> 4.56 mm
- net Net-(JP602-Pad1): track 0.00 -> 4.41 mm
- net /Core/[SCL3_uC]: track 46.0 -> 48.2 mm, vias 1 -> 3
- net /Core/[SDA3_uC]: track 47.0 -> 46.0 mm
- net Net-(Q606-Pad2): track 22.4 -> 21.9 mm

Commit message: Version 1.0 compra en jlcpcb.
    *Se agregan gerbers e ibom de version de produccion.
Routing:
- net +5V: track 390.9 -> 448.2 mm
- net GND: track 1300.4 -> 1282.9 mm, vias 123 -> 121
- added copper zone on F.Cu, net +5V
